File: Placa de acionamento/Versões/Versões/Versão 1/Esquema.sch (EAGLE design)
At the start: 23 parts, among them Q1 IRF540, Q2 IRF540, Q3 IRF540

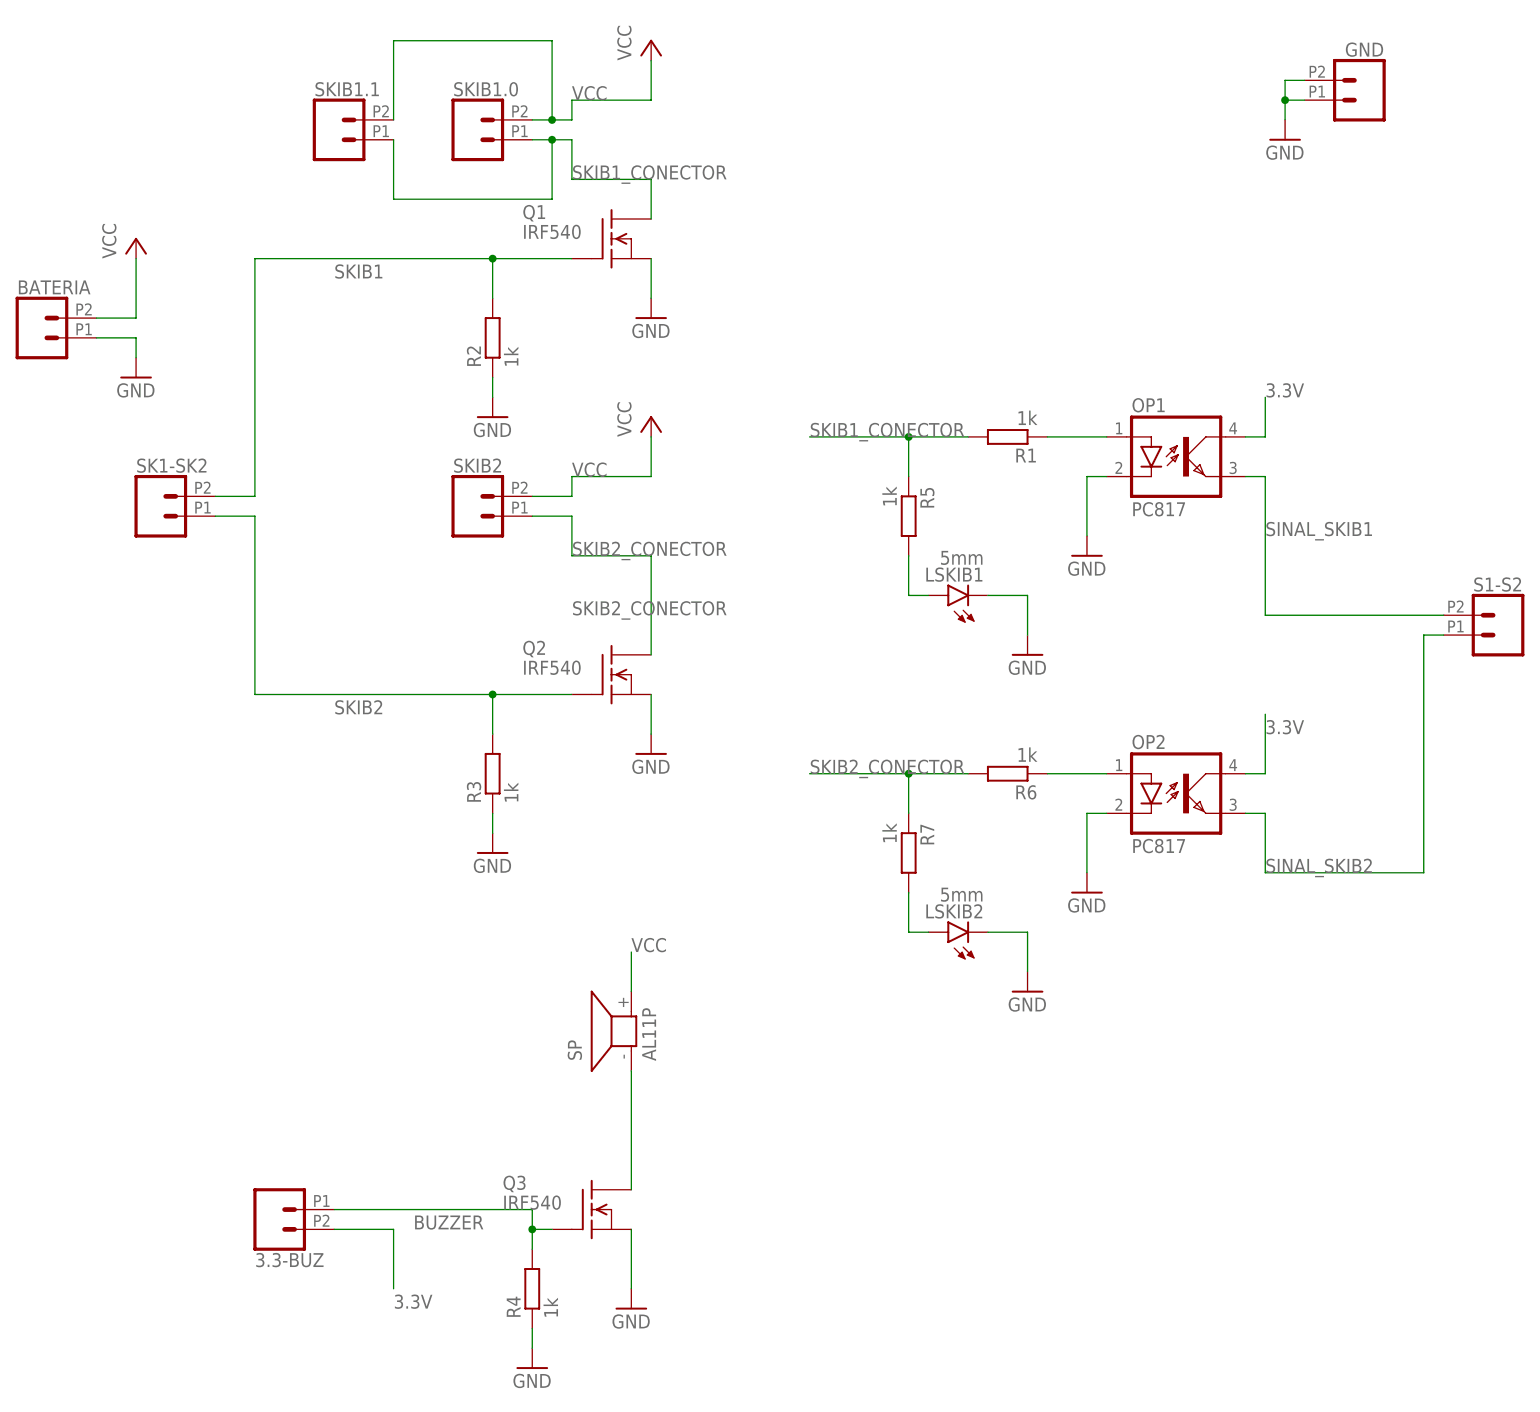
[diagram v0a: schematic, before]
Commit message: CHORE: adicionando modelos 3D
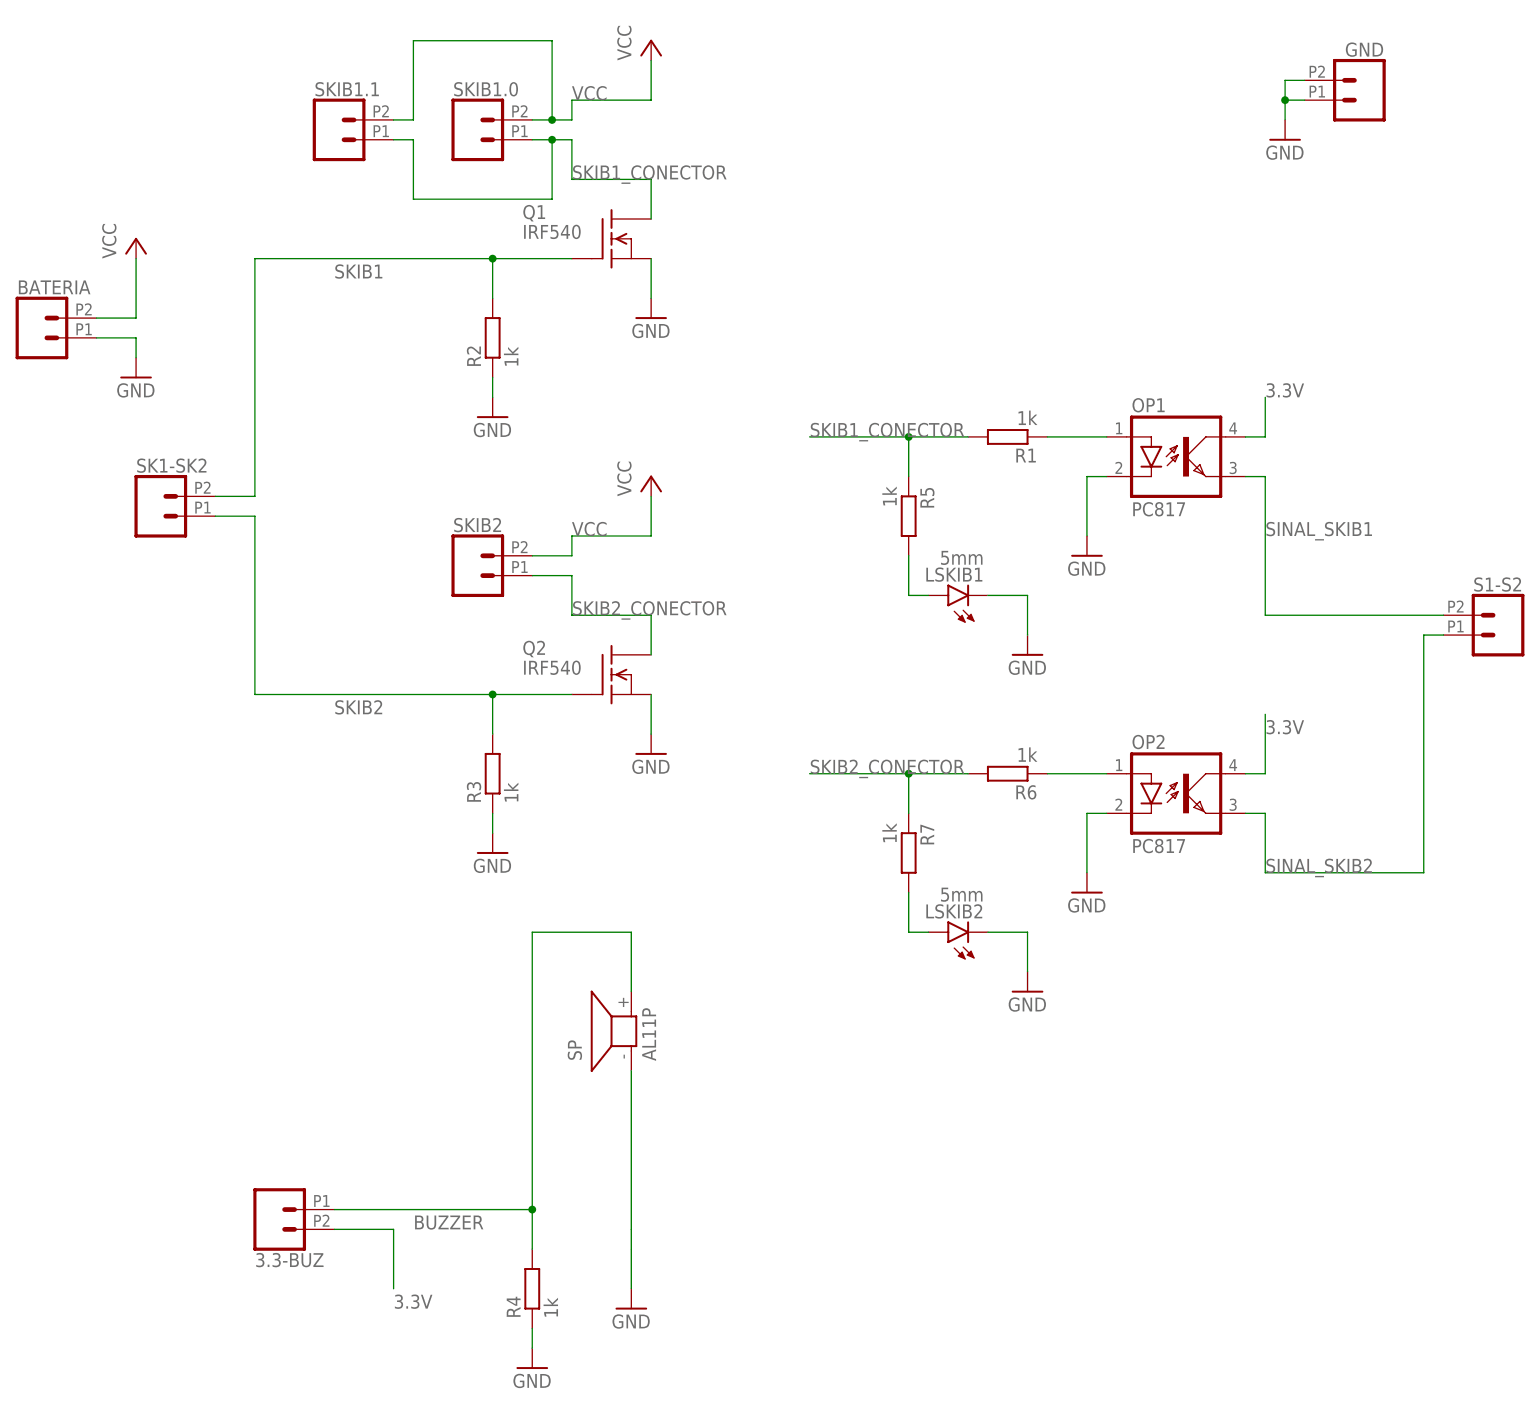
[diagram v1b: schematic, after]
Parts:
- removed Q3: IRF540, transistor-fet:IRF540
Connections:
- removed net N$2: Q3.D, SP.1
- net BUZZER: now also SP.2; no longer Q3.G
- net GND: now also SP.1; no longer Q3.S
- net VCC: no longer SP.2
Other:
- moved on the sheet: SKIB2
